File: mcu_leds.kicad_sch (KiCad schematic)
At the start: 11 parts, among them U54 SN74LVC1G07DCKR

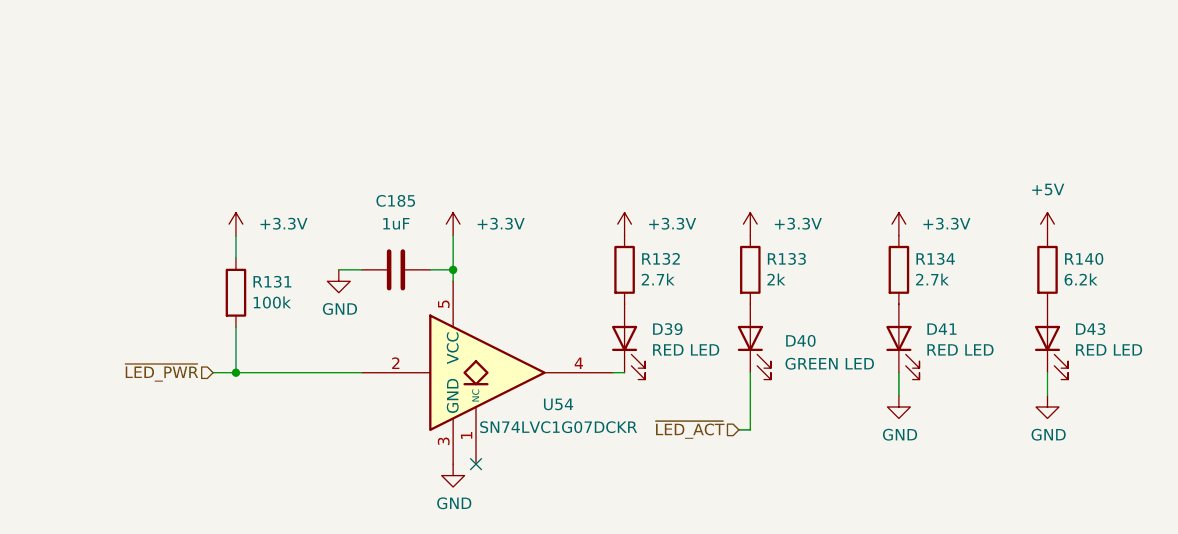
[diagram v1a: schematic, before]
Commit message: Add a clock oscillator for NVMe SUSCLK
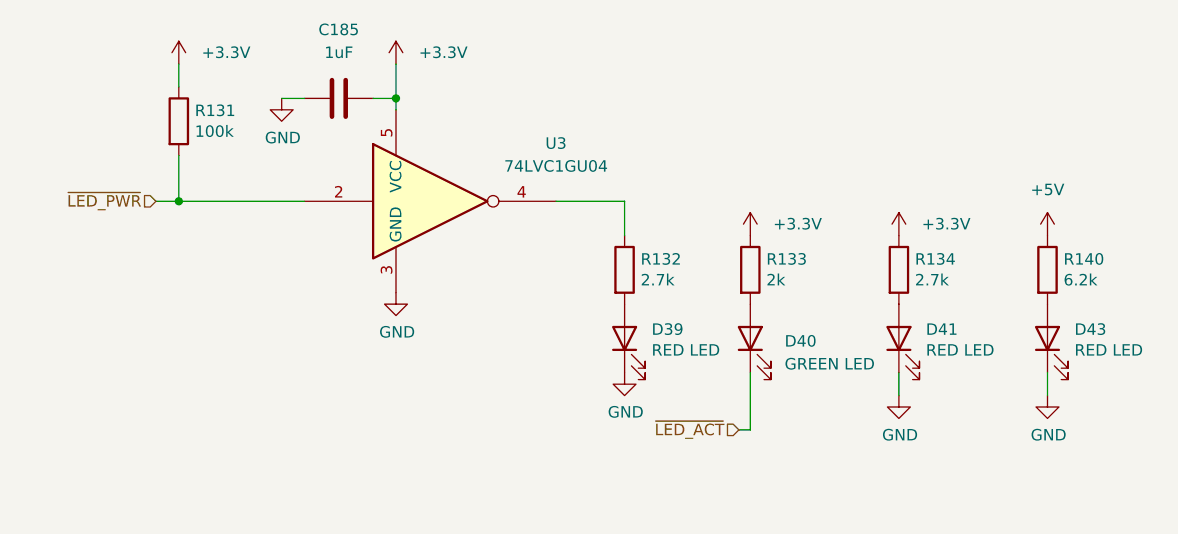
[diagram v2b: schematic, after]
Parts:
- removed U54: SN74LVC1G07DCKR, Package_TO_SOT_SMD:SOT-353_SC-70-5, symbol 74xGxx:74LVC1G07
- added U3: 74LVC1GU04, Package_TO_SOT_SMD:SOT-353_SC-70-5, symbol 74xGxx:74LVC1GU04
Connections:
- net +3.3V: now also U3.5 (VCC); no longer R132.1
- net GND: now also D39.1 (K), U3.3 (GND)
- net ~{LED_PWR}: now also U3.2
- new net: R132.1, U3.4
- no-connect marks 1 -> 0
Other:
- moved on the sheet: C185, R131

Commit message: Update JLCPCB corrections
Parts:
- U3: JLCPCB_CORRECTION (none) -> 0;0;270
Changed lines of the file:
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@@
+			)
+		)
+		(property "JLCPCB_CORRECTION" "0;0;270"
+			(at 118.11 76.2 0)
+			(effects
+				(font
+					(size 1.27 1.27)
+				)
+				(hide yes)
 			)
 		)
